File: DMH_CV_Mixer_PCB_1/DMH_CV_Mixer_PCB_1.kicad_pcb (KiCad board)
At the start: 2 copper layers, 48 x 175 mm, 0 parts

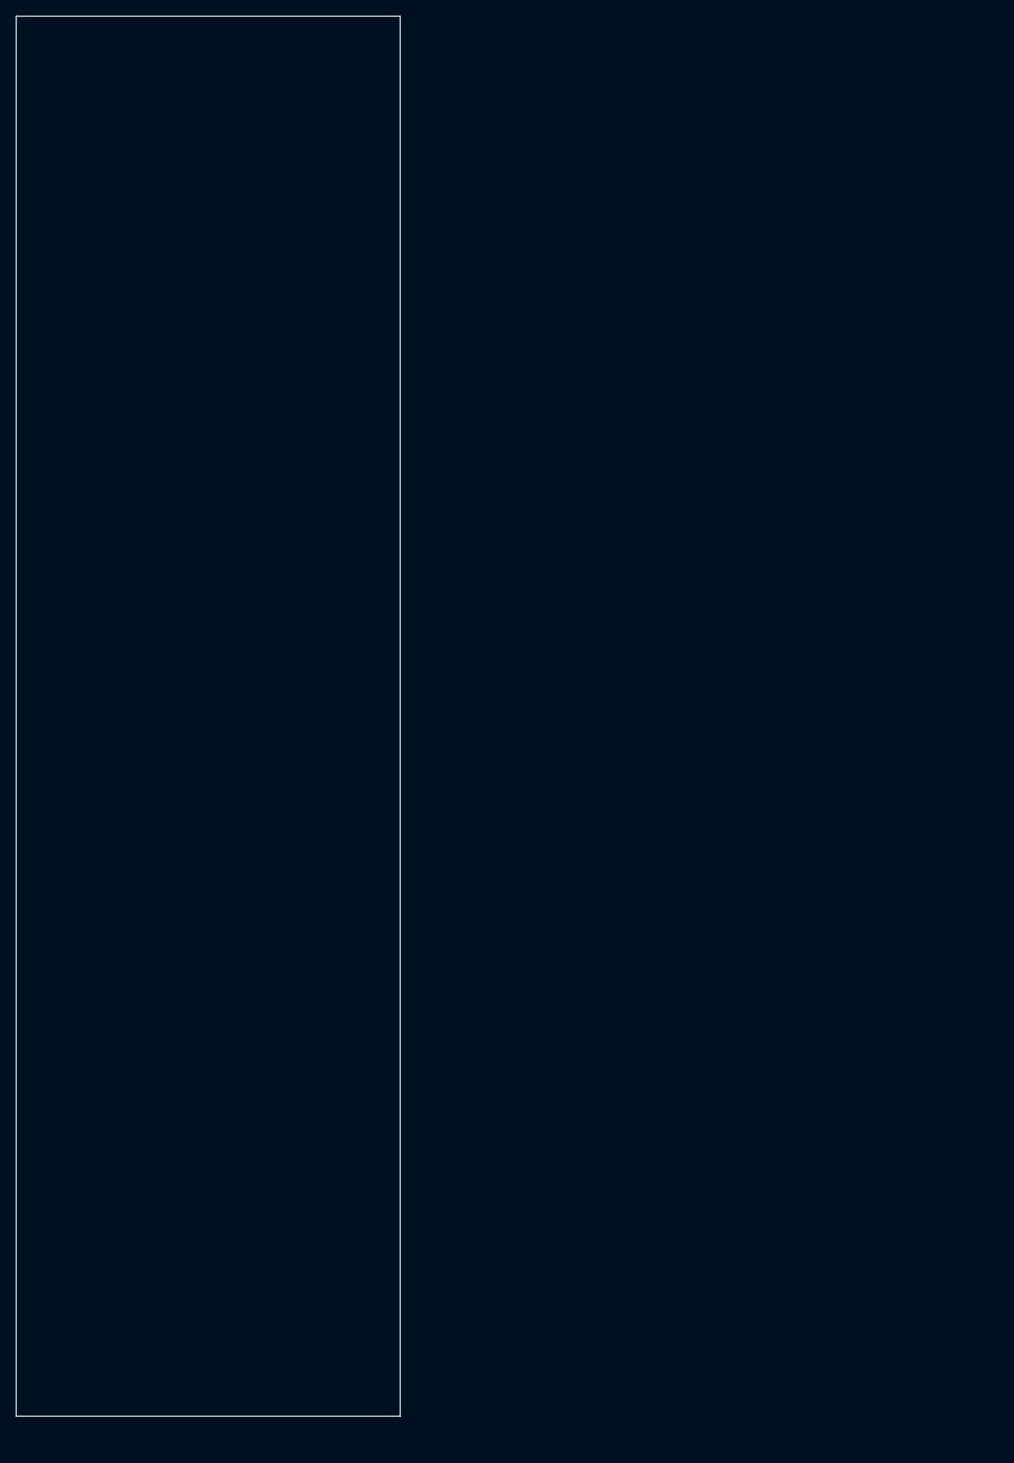
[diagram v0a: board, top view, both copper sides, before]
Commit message: Started IO part design
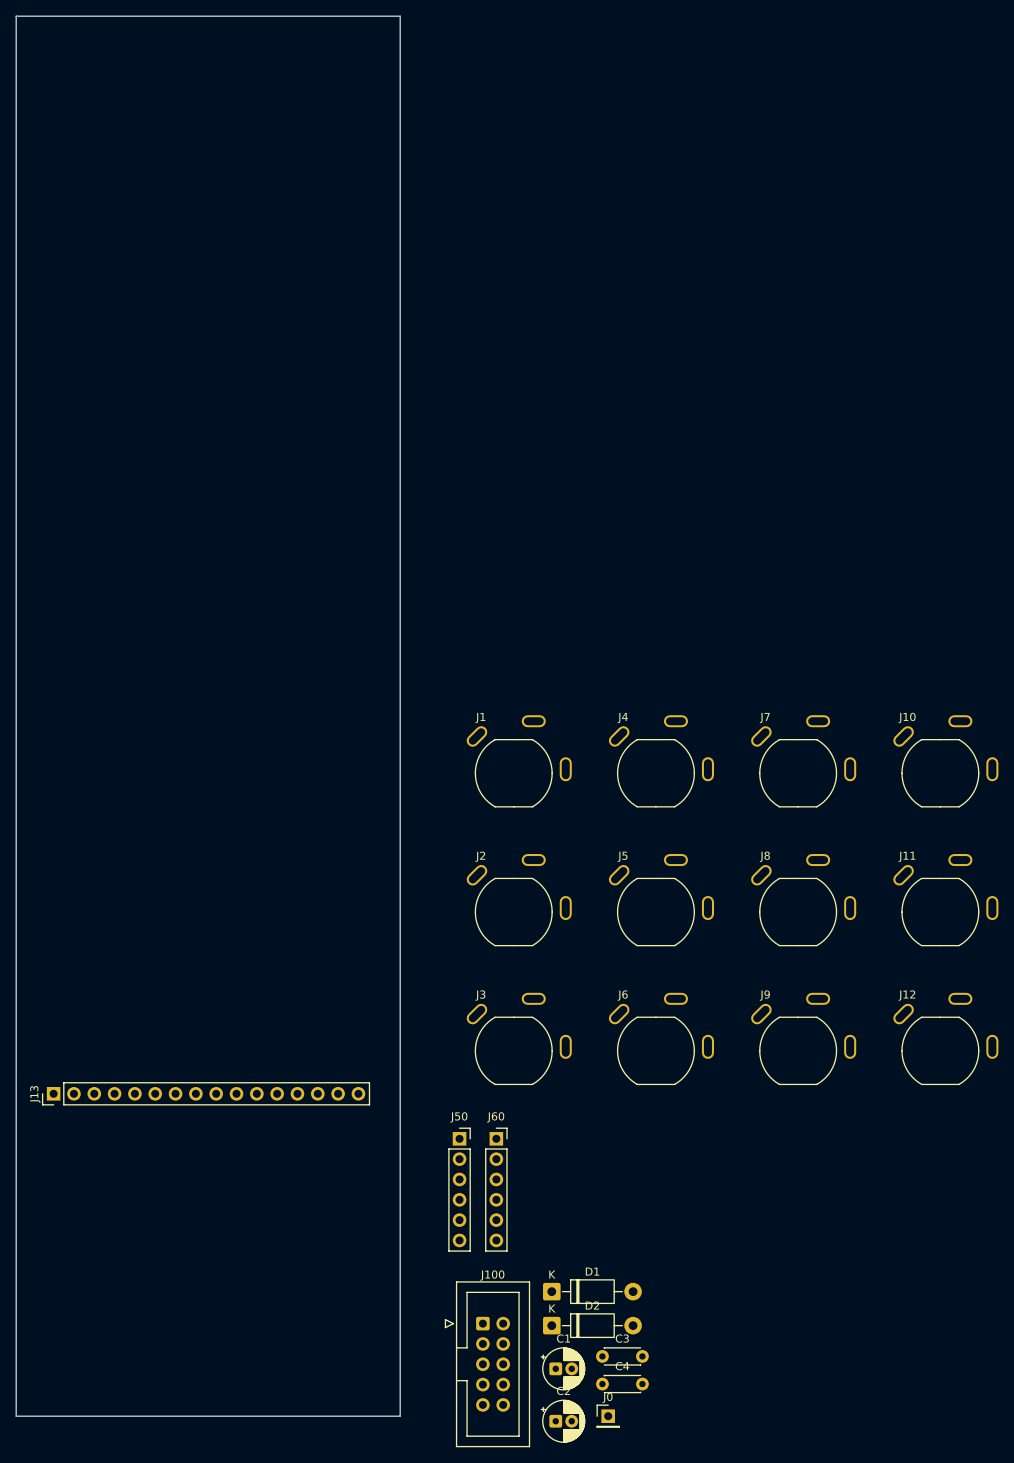
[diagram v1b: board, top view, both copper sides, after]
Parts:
- added C1: 47uF, Capacitor_THT:CP_Radial_D5.0mm_P2.00mm, F.Cu at (118.4, 211.6)
- added C2: 47uF, Capacitor_THT:CP_Radial_D5.0mm_P2.00mm, F.Cu at (118.4, 218.1)
- added C3: 100nF, Capacitor_THT:C_Disc_D4.3mm_W1.9mm_P5.00mm, F.Cu at (124.3, 210.0)
- added C4: 100nF, Capacitor_THT:C_Disc_D4.3mm_W1.9mm_P5.00mm, F.Cu at (124.3, 213.5)
- added D1: SB140+, Diode_THT:D_DO-41_SOD81_P10.16mm_Horizontal, F.Cu at (118.0, 201.9)
- added D2: SB140-, Diode_THT:D_DO-41_SOD81_P10.16mm_Horizontal, F.Cu at (118.0, 206.2)
- added J0: Conn_01x01, Connector_PinHeader_2.54mm:PinHeader_1x01_P2.54mm_Vertical, F.Cu at (125.0, 217.5)
- added J1: TS_Jack_6.35mm_Sw, SynthStuff:CUI_MJ-63052A, F.Cu at (113.2, 137.1)
- added J10: TS_Jack_6.35mm_Sw, SynthStuff:CUI_MJ-63052A, F.Cu at (166.5, 137.1)
- added J100: IDC_02x05, SynthStuff:IDC-Header_2x05_P2.54mm_Vertical_Eurorack, F.Cu at (109.3, 205.9)
- added J11: TS_Jack_6.35mm_Sw, SynthStuff:CUI_MJ-63052A, F.Cu at (166.5, 154.5)
- added J12: TS_Jack_6.35mm_Sw, SynthStuff:CUI_MJ-63052A, F.Cu at (166.5, 171.8)
- added J13: Conn_01x16, Connector_PinHeader_2.54mm:PinHeader_1x16_P2.54mm_Vertical, F.Cu at (55.7, 177.2)
- added J2: TS_Jack_6.35mm_Sw, SynthStuff:CUI_MJ-63052A, F.Cu at (113.2, 154.5)
- added J3: TS_Jack_6.35mm_Sw, SynthStuff:CUI_MJ-63052A, F.Cu at (113.2, 171.8)
- added J4: TS_Jack_6.35mm_Sw, SynthStuff:CUI_MJ-63052A, F.Cu at (131.0, 137.1)
- added J5: TS_Jack_6.35mm_Sw, SynthStuff:CUI_MJ-63052A, F.Cu at (131.0, 154.5)
- added J50: Conn_01x06, Connector_PinSocket_2.54mm:PinSocket_1x06_P2.54mm_Vertical, F.Cu at (106.4, 182.8)
- added J6: TS_Jack_6.35mm_Sw, SynthStuff:CUI_MJ-63052A, F.Cu at (131.0, 171.8)
- added J60: Conn_01x06, Connector_PinSocket_2.54mm:PinSocket_1x06_P2.54mm_Vertical, F.Cu at (111.0, 182.8)
- added J7: TS_Jack_6.35mm_Sw, SynthStuff:CUI_MJ-63052A, F.Cu at (148.7, 137.1)
- added J8: TS_Jack_6.35mm_Sw, SynthStuff:CUI_MJ-63052A, F.Cu at (148.7, 154.5)
- added J9: TS_Jack_6.35mm_Sw, SynthStuff:CUI_MJ-63052A, F.Cu at (148.7, 171.8)
